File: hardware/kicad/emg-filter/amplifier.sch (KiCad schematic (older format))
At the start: 40 parts, among them U1 LM4565, U2 LM4565, U3 LM4565, U4 LM4565, U5 LM4565, U6 LM4565, U7 LM4565, U8 LM4565

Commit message: annotation
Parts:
- renumbered R1 to R235, R2 to R236, R5 to R237, R6 to R238, R7 to R239, R8 to R240, R3 to R241, R4 to R242, R9 to R243, R10 to R244, R11 to R245, R12 to R246, R13 to R247, R14 to R248, R15 to R249, R16 to R250, R17 to R251, R18 to R252, R19 to R253, R20 to R254, R21 to R255, R22 to R256, R23 to R257, R24 to R258, R25 to R259, R26 to R260, R27 to R261, R28 to R262, R29 to R263, R30 to R264, R31 to R265, R32 to R266, U1 to U52, U2 to U53, U3 to U54, U4 to U55, U5 to U56, U6 to U57, U7 to U58, U8 to U59

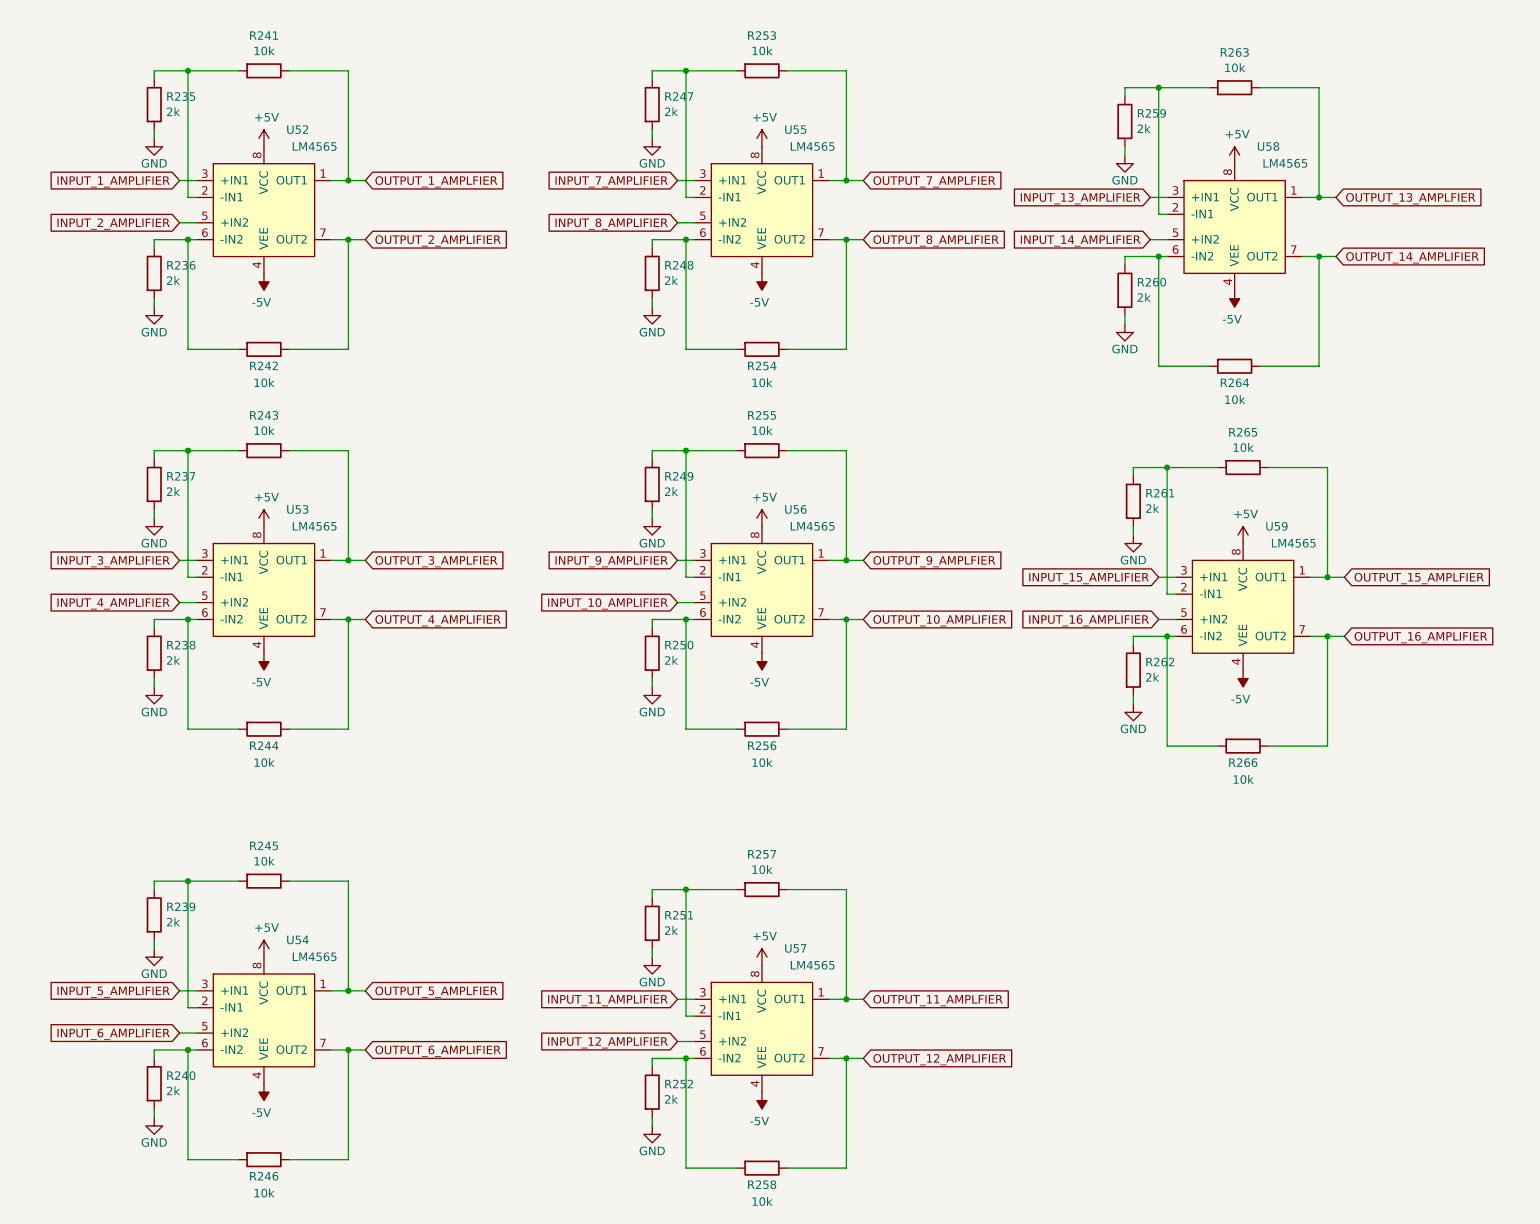
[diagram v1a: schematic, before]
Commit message: linked stages by renaming labels
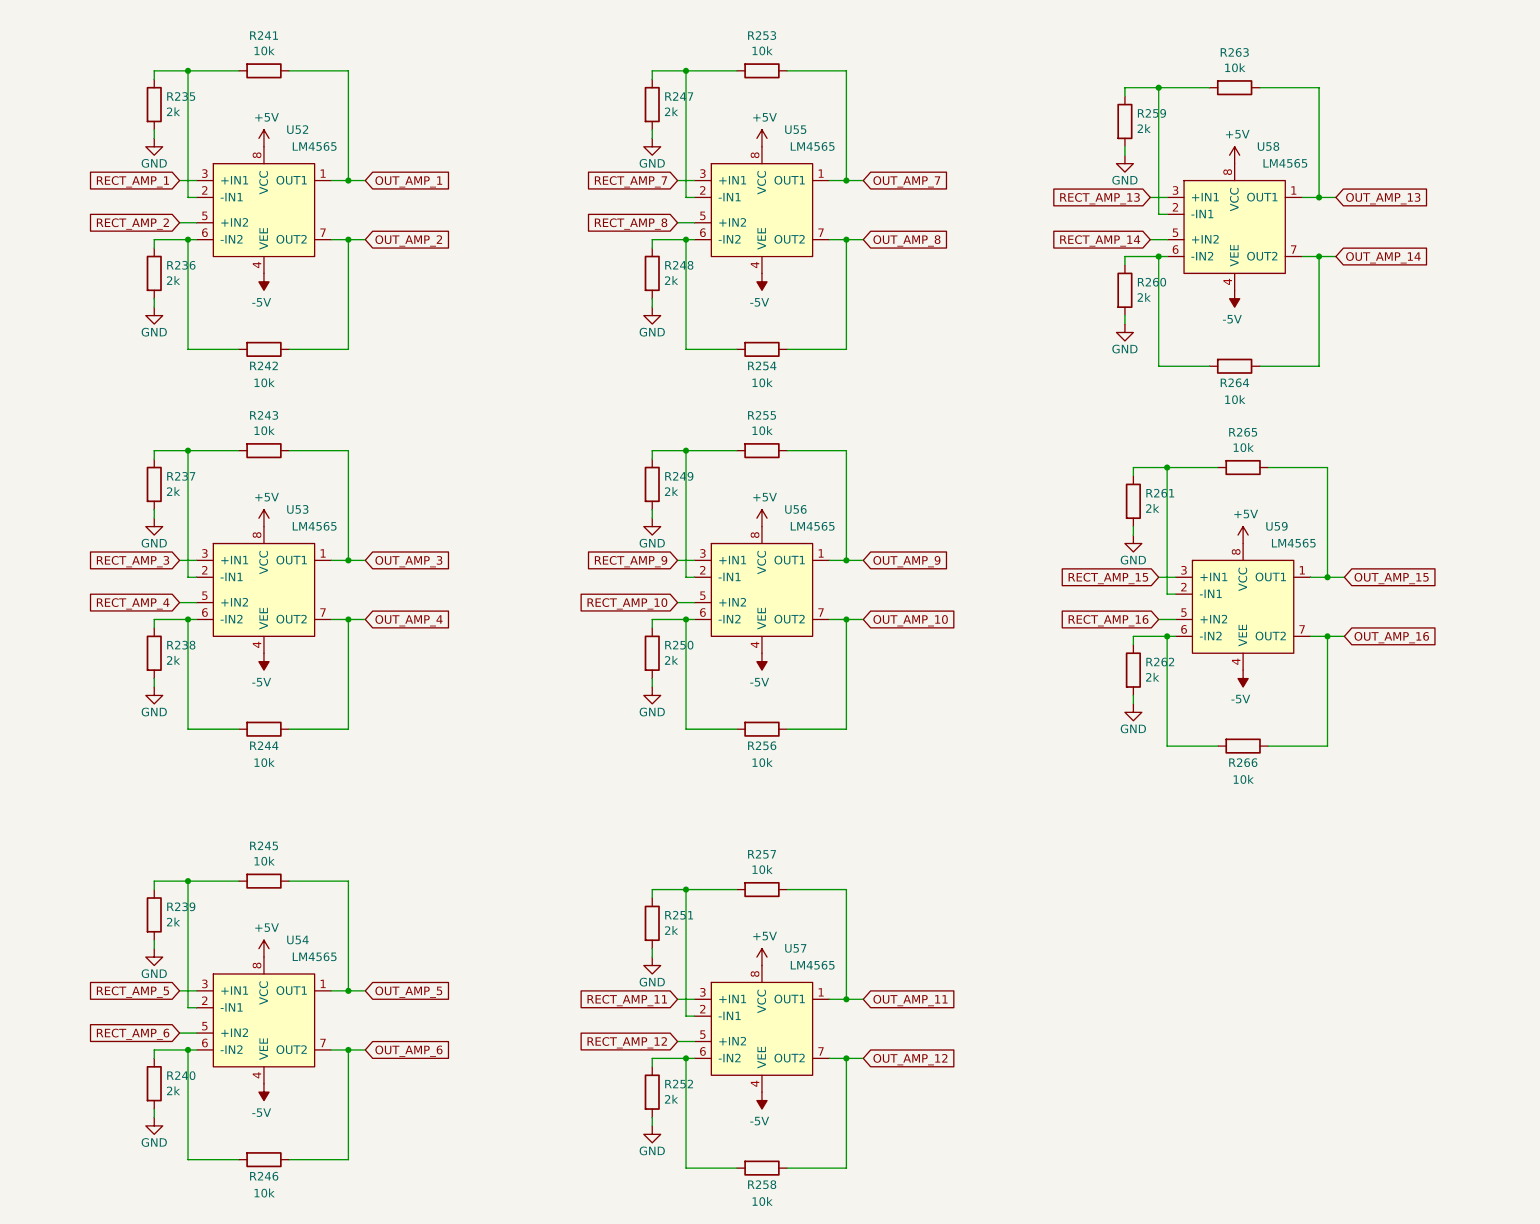
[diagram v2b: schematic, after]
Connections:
- net INPUT_10_AMPLIFIER renamed RECT_AMP_10
- net INPUT_11_AMPLIFIER renamed RECT_AMP_11
- net INPUT_12_AMPLIFIER renamed RECT_AMP_12
- net INPUT_13_AMPLIFIER renamed RECT_AMP_13
- net INPUT_14_AMPLIFIER renamed RECT_AMP_14
- net INPUT_15_AMPLIFIER renamed RECT_AMP_15
- net INPUT_16_AMPLIFIER renamed RECT_AMP_16
- net INPUT_1_AMPLIFIER renamed RECT_AMP_1
- net INPUT_2_AMPLIFIER renamed RECT_AMP_2
- net INPUT_3_AMPLIFIER renamed RECT_AMP_3
- net INPUT_4_AMPLIFIER renamed RECT_AMP_4
- net INPUT_5_AMPLIFIER renamed RECT_AMP_5
- net INPUT_6_AMPLIFIER renamed RECT_AMP_6
- net INPUT_7_AMPLIFIER renamed RECT_AMP_7
- net INPUT_8_AMPLIFIER renamed RECT_AMP_8
- net INPUT_9_AMPLIFIER renamed RECT_AMP_9
- net OUTPUT_10_AMPLIFIER renamed OUT_AMP_10
- net OUTPUT_11_AMPLFIER renamed OUT_AMP_11
- net OUTPUT_12_AMPLIFIER renamed OUT_AMP_12
- net OUTPUT_13_AMPLFIER renamed OUT_AMP_13
- net OUTPUT_14_AMPLIFIER renamed OUT_AMP_14
- net OUTPUT_15_AMPLFIER renamed OUT_AMP_15
- net OUTPUT_16_AMPLIFIER renamed OUT_AMP_16
- net OUTPUT_1_AMPLFIER renamed OUT_AMP_1
- net OUTPUT_2_AMPLIFIER renamed OUT_AMP_2
- net OUTPUT_3_AMPLFIER renamed OUT_AMP_3
- net OUTPUT_4_AMPLIFIER renamed OUT_AMP_4
- net OUTPUT_5_AMPLFIER renamed OUT_AMP_5
- net OUTPUT_6_AMPLIFIER renamed OUT_AMP_6
- net OUTPUT_7_AMPLFIER renamed OUT_AMP_7
- net OUTPUT_8_AMPLIFIER renamed OUT_AMP_8
- net OUTPUT_9_AMPLFIER renamed OUT_AMP_9
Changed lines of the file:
@@
 $Descr A4 11693 8268
 encoding utf-8
-Sheet 1 10
+Sheet 8 10
 Title ""
 Date ""
@@
 	1    0    0    -1
 $EndComp
-Text GLabel 1300 1750 0    50   Input ~ 0
-INPUT_2_AMPLIFIER
 $Comp
 L Device:R R241
@@
 Wire Wire Line
 	1350 1850 1350 2500
-Text GLabel 2400 1850 2    50   Input ~ 0
-OUTPUT_2_AMPLIFIER
 Wire Wire Line
 	2400 1850 2300 1850
 Connection ~ 2300 1850
 Text GLabel 2400 1500 2    50   Input ~ 0
-OUTPUT_1_AMPLFIER
+OUT_AMP_1
 Wire Wire Line
 	2300 1500 2400 1500
@@
 Wire Wire Line
 	1150 850  1150 900
-Text GLabel 1300 1500 0    50   Input ~ 0
-INPUT_1_AMPLIFIER
 Wire Wire Line
 	1150 1200 1150 1250
@@
 	1    0    0    -1
 $EndComp
-Text GLabel 1300 4000 0    50   Input ~ 0
-INPUT_4_AMPLIFIER
 $Comp
 L Device:R R243
@@
 Wire Wire Line
 	1350 4100 1350 4750
-Text GLabel 2400 4100 2    50   Input ~ 0
-OUTPUT_4_AMPLIFIER
 Wire Wire Line
 	2400 4100 2300 4100
 Connection ~ 2300 4100
-Text GLabel 2400 3750 2    50   Input ~ 0
-OUTPUT_3_AMPLFIER
 Wire Wire Line
 	2300 3750 2400 3750
@@
 Wire Wire Line
 	1150 3100 1150 3150
-Text GLabel 1300 3750 0    50   Input ~ 0
-INPUT_3_AMPLIFIER
 Wire Wire Line
 	1150 3450 1150 3500
@@
 	1    0    0    -1
 $EndComp
-Text GLabel 4250 1750 0    50   Input ~ 0
-INPUT_8_AMPLIFIER
 $Comp
 L Device:R R253
@@
 Wire Wire Line
 	4300 1850 4300 2500
-Text GLabel 5350 1850 2    50   Input ~ 0
-OUTPUT_8_AMPLIFIER
 Wire Wire Line
 	5350 1850 5250 1850
 Connection ~ 5250 1850
-Text GLabel 5350 1500 2    50   Input ~ 0
-OUTPUT_7_AMPLFIER
 Wire Wire Line
 	5250 1500 5350 1500
@@
 Wire Wire Line
 	4100 850  4100 900
-Text GLabel 4250 1500 0    50   Input ~ 0
-INPUT_7_AMPLIFIER
 Wire Wire Line
 	4100 1200 4100 1250
@@
 	1    0    0    -1
 $EndComp
-Text GLabel 4250 4000 0    50   Input ~ 0
-INPUT_10_AMPLIFIER
 $Comp
 L Device:R R255
@@
 Wire Wire Line
 	4300 4100 4300 4750
-Text GLabel 5350 4100 2    50   Input ~ 0
-OUTPUT_10_AMPLIFIER
 Wire Wire Line
 	5350 4100 5250 4100
 Connection ~ 5250 4100
-Text GLabel 5350 3750 2    50   Input ~ 0
-OUTPUT_9_AMPLFIER
 Wire Wire Line
 	5250 3750 5350 3750
@@
 Wire Wire Line
 	4100 3100 4100 3150
-Text GLabel 4250 3750 0    50   Input ~ 0
-INPUT_9_AMPLIFIER
 Wire Wire Line
 	4100 3450 4100 3500
@@
 	1    0    0    -1
 $EndComp
-Text GLabel 7050 1850 0    50   Input ~ 0
-INPUT_14_AMPLIFIER
 $Comp
 L Device:R R263
@@
 Wire Wire Line
 	7100 1950 7100 2600
-Text GLabel 8150 1950 2    50   Input ~ 0
-OUTPUT_14_AMPLIFIER
 Wire Wire Line
 	8150 1950 8050 1950
 Connection ~ 8050 1950
-Text GLabel 8150 1600 2    50   Input ~ 0
-OUTPUT_13_AMPLFIER
 Wire Wire Line
 	8050 1600 8150 1600
@@
 Wire Wire Line
 	6900 950  6900 1000
-Text GLabel 7050 1600 0    50   Input ~ 0
-INPUT_13_AMPLIFIER
 Wire Wire Line
 	6900 1300 6900 1350
@@
 	1    0    0    -1
 $EndComp
-Text GLabel 7100 4100 0    50   Input ~ 0
-INPUT_16_AMPLIFIER
 $Comp
 L Device:R R265
@@
 Wire Wire Line
 	7150 4200 7150 4850
-Text GLabel 8200 4200 2    50   Input ~ 0
-OUTPUT_16_AMPLIFIER
 Wire Wire Line
 	8200 4200 8100 4200
 Connection ~ 8100 4200
-Text GLabel 8200 3850 2    50   Input ~ 0
-OUTPUT_15_AMPLFIER
 Wire Wire Line
 	8100 3850 8200 3850
@@
 Wire Wire Line
 	6950 3200 6950 3250
-Text GLabel 7100 3850 0    50   Input ~ 0
-INPUT_15_AMPLIFIER
 Wire Wire Line
 	6950 3550 6950 3600
@@
 	1    0    0    -1
 $EndComp
-Text GLabel 1300 6550 0    50   Input ~ 0
-INPUT_6_AMPLIFIER
 $Comp
 L Device:R R245
@@
 Wire Wire Line
 	1350 6650 1350 7300
-Text GLabel 2400 6650 2    50   Input ~ 0
-OUTPUT_6_AMPLIFIER
 Wire Wire Line
 	2400 6650 2300 6650
 Connection ~ 2300 6650
-Text GLabel 2400 6300 2    50   Input ~ 0
-OUTPUT_5_AMPLFIER
 Wire Wire Line
 	2300 6300 2400 6300
@@
 Wire Wire Line
 	1150 5650 1150 5700
-Text GLabel 1300 6300 0    50   Input ~ 0
-INPUT_5_AMPLIFIER
 Wire Wire Line
 	1150 6000 1150 6050
@@
 	1    0    0    -1
 $EndComp
-Text GLabel 4250 6600 0    50   Input ~ 0
-INPUT_12_AMPLIFIER
 $Comp
 L Device:R R257
@@
 Wire Wire Line
 	4300 6700 4300 7350
-Text GLabel 5350 6700 2    50   Input ~ 0
-OUTPUT_12_AMPLIFIER
 Wire Wire Line
 	5350 6700 5250 6700
 Connection ~ 5250 6700
-Text GLabel 5350 6350 2    50   Input ~ 0
-OUTPUT_11_AMPLFIER
 Wire Wire Line
 	5250 6350 5350 6350
@@
 Wire Wire Line
 	4100 5700 4100 5750
-Text GLabel 4250 6350 0    50   Input ~ 0
-INPUT_11_AMPLIFIER
 Wire Wire Line
 	4100 6050 4100 6100
@@
 Wire Wire Line
 	4350 6600 4250 6600
+Text GLabel 1300 1500 0    50   Input ~ 0
+RECT_AMP_1
+Text GLabel 1300 1750 0    50   Input ~ 0
+RECT_AMP_2
+Text GLabel 1300 3750 0    50   Input ~ 0
+RECT_AMP_3
+Text GLabel 1300 4000 0    50   Input ~ 0
+RECT_AMP_4
+Text GLabel 1300 6300 0    50   Input ~ 0
+RECT_AMP_5
+Text GLabel 1300 6550 0    50   Input ~ 0
+RECT_AMP_6
+Text GLabel 4250 1500 0    50   Input ~ 0
+RECT_AMP_7
+Text GLabel 4250 1750 0    50   Input ~ 0
+RECT_AMP_8
+Text GLabel 4250 3750 0    50   Input ~ 0
+RECT_AMP_9
+Text GLabel 4250 4000 0    50   Input ~ 0
+RECT_AMP_10
+Text GLabel 4250 6350 0    50   Input ~ 0
+RECT_AMP_11
+Text GLabel 4250 6600 0    50   Input ~ 0
+RECT_AMP_12
+Text GLabel 7050 1600 0    50   Input ~ 0
+RECT_AMP_13
+Text GLabel 7050 1850 0    50   Input ~ 0
+RECT_AMP_14
+Text GLabel 7100 3850 0    50   Input ~ 0
+RECT_AMP_15
+Text GLabel 7100 4100 0    50   Input ~ 0
+RECT_AMP_16
+Text GLabel 2400 1850 2    50   Input ~ 0
+OUT_AMP_2
+Text GLabel 2400 3750 2    50   Input ~ 0
+OUT_AMP_3
+Text GLabel 2400 4100 2    50   Input ~ 0
+OUT_AMP_4
+Text GLabel 2400 6300 2    50   Input ~ 0
+OUT_AMP_5
+Text GLabel 2400 6650 2    50   Input ~ 0
+OUT_AMP_6
+Text GLabel 8200 4200 2    50   Input ~ 0
+OUT_AMP_16
+Text GLabel 8200 3850 2    50   Input ~ 0
+OUT_AMP_15
+Text GLabel 8150 1950 2    50   Input ~ 0
+OUT_AMP_14
+Text GLabel 8150 1600 2    50   Input ~ 0
+OUT_AMP_13
+Text GLabel 5350 6700 2    50   Input ~ 0
+OUT_AMP_12
+Text GLabel 5350 6350 2    50   Input ~ 0
+OUT_AMP_11
+Text GLabel 5350 4100 2    50   Input ~ 0
+OUT_AMP_10
+Text GLabel 5350 3750 2    50   Input ~ 0
+OUT_AMP_9
+Text GLabel 5350 1850 2    50   Input ~ 0
+OUT_AMP_8
+Text GLabel 5350 1500 2    50   Input ~ 0
+OUT_AMP_7
 $EndSCHEMATC

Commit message: notes from review with Dmitry, 01-06-22
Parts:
- added POT: 10k, symbol Device:R
- added R?: Same as inverting 2k (inverting branch), symbol Device:R
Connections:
- net OUT_AMP_2: now also POT.1
- net RECT_AMP_1: now also R?.1; no longer U52.3 (+IN1)
- net at R236.1, R242.2, U52.6 (-IN2): now also POT.2
- new net: R?.2, U52.3 (+IN1)
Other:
- note added: "Consider POT for few stages, add jumpers, multiturn for resolution"
- note added: "rEPLACE WITH OUR VIRTUAL gnd, can potentiallly provide negative voltage"
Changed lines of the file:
@@
 $EndComp
 Wire Wire Line
-	1350 2500 1650 2500
-Wire Wire Line
-	1950 2500 2300 2500
+	1350 2500 1550 2500
+Wire Wire Line
+	1950 2500 2050 2500
 $Comp
 L power:-5V #PWR0179
@@
 Wire Wire Line
 	4350 6600 4250 6600
-Text GLabel 1300 1500 0    50   Input ~ 0
+Text GLabel 1100 1500 0    50   Input ~ 0
 RECT_AMP_1
 Text GLabel 1300 1750 0    50   Input ~ 0
@@
 Text GLabel 5350 1500 2    50   Input ~ 0
 OUT_AMP_7
+Text Notes 2000 2100 0    50   ~ 0
+rEPLACE WITH OUR VIRTUAL gnd, can potentiallly provide negative voltage
+$Comp
+L Device:R R?
+U 1 1 61EBAAA0
+P 1250 1500
+F 0 "R?" V 1457 1500 50  0000 C CNN
+F 1 "Same as inverting 2k (inverting branch)" V 1366 1500 50  0000 C CNN
+F 2 "" V 1180 1500 50  0001 C CNN
+F 3 "~" H 1250 1500 50  0001 C CNN
+	1    1250 1500
+	0    -1   -1   0
+$EndComp
+Connection ~ 1400 1500
+Text Notes 850  600  0    50   ~ 0
+Consider POT for few stages, add jumpers, multiturn for resolution
+$Comp
+L Device:R POT
+U 1 1 61EBE9EC
+P 1800 2350
+F 0 "POT" V 1900 2350 50  0000 C CNN
+F 1 "10k" V 2000 2350 50  0000 C CNN
+F 2 "" V 1730 2350 50  0001 C CNN
+F 3 "~" H 1800 2350 50  0001 C CNN
+	1    1800 2350
+	0    1    1    0
+$EndComp
+Wire Wire Line
+	1650 2350 1550 2350
+Wire Wire Line
+	1550 2350 1550 2500
+Connection ~ 1550 2500
+Wire Wire Line
+	1550 2500 1650 2500
+Wire Wire Line
+	1950 2350 2050 2350
+Wire Wire Line
+	2050 2350 2050 2500
+Connection ~ 2050 2500
+Wire Wire Line
+	2050 2500 2300 2500
 $EndSCHEMATC
